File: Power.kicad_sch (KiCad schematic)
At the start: 5 parts, among them U4 LD1117S33TR_SOT223

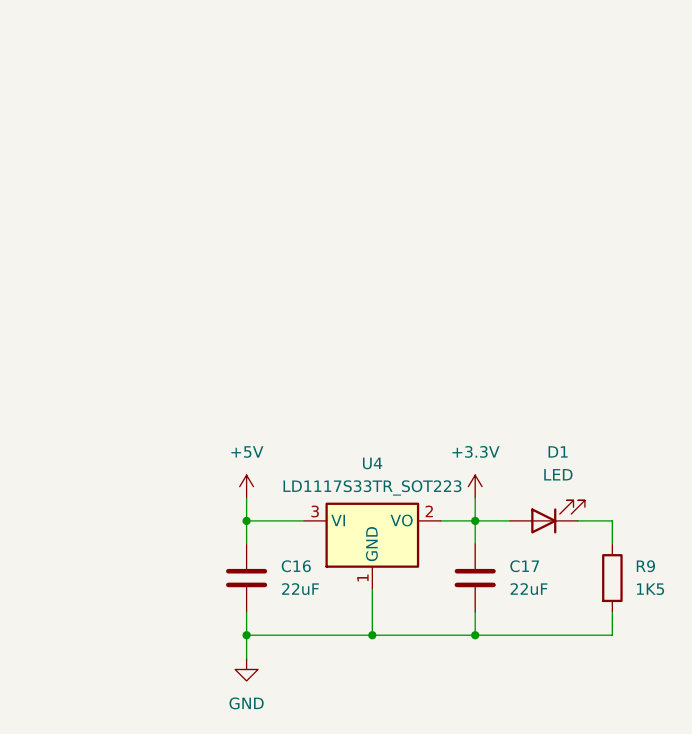
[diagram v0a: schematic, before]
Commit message: MOD : KiCad 8.0.1 -> 9.0.0. ADD : Codec power circuitry.
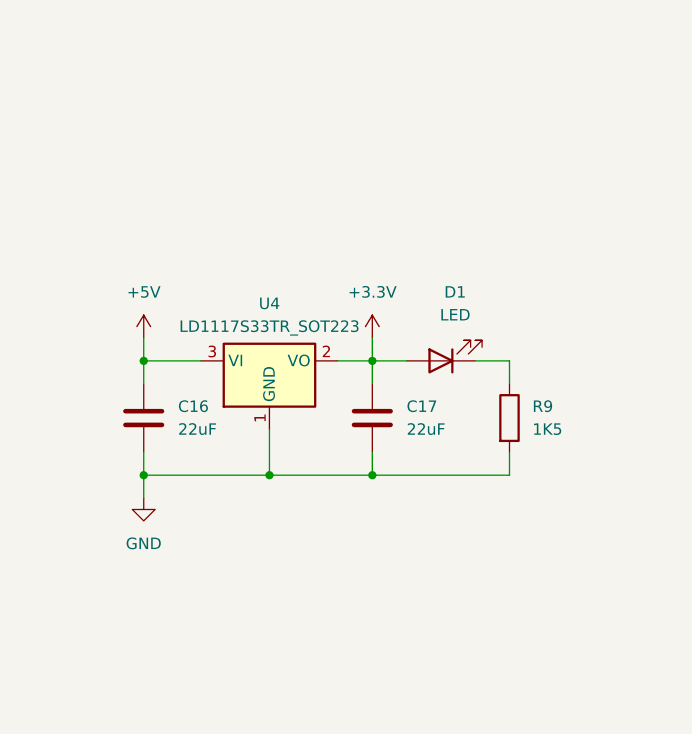
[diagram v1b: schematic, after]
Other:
- moved on the sheet: C16, C17, D1, R9, U4

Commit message: ADD : Footprint assignment. FIX : Various ERC rules.
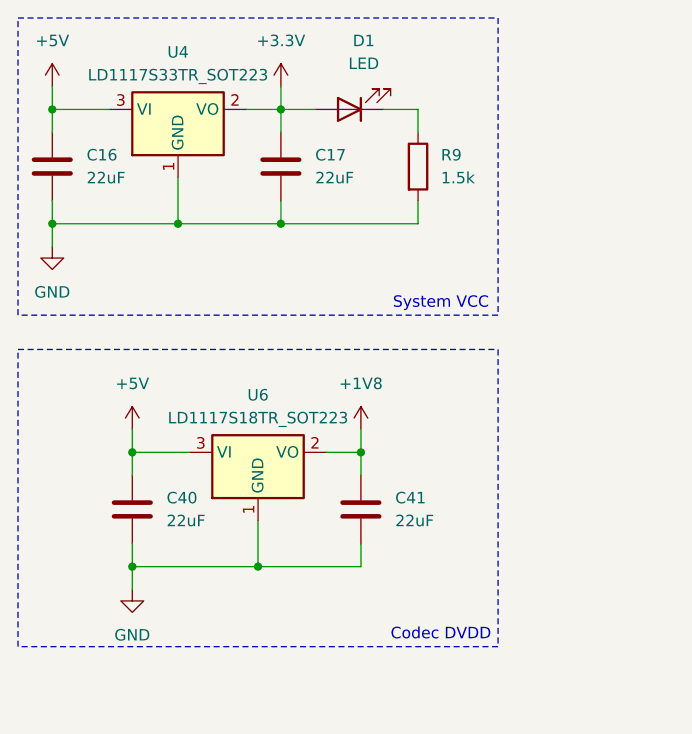
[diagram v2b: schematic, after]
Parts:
- added C40, C41: 22uF, Capacitor_SMD:C_0402_1005Metric, symbol Device:C
- added U6: LD1117S18TR_SOT223, Package_TO_SOT_SMD:SOT-223-3_TabPin2, symbol Regulator_Linear:LD1117S18TR_SOT223
- C16, C17: footprint (none) -> Capacitor_SMD:C_0402_1005Metric
- D1: footprint (none) -> LED_SMD:LED_0402_1005Metric
- R9: value 1K5 -> 1.5k; footprint (none) -> Resistor_SMD:R_0402_1005Metric
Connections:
- net +5V: now also C40.1, U6.3 (VI)
- net GND: now also C40.2, C41.2, U6.1 (GND)
- new net +1V8: C41.1, U6.2 (VO)
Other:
- note added: "Codec DVDD"
- note added: "System VCC"
- moved on the sheet: C16, C17, D1, R9, U4

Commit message: ADD : Rough PCB part placement. MOD : Swapped codec DVDD LDO.
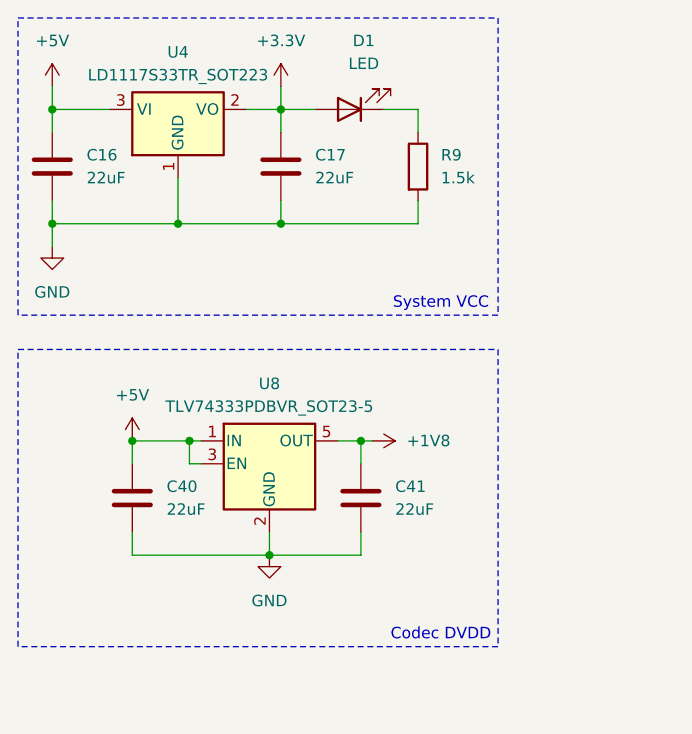
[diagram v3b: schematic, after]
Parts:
- removed U6: LD1117S18TR_SOT223, Package_TO_SOT_SMD:SOT-223-3_TabPin2, symbol Regulator_Linear:LD1117S18TR_SOT223
- added U8: TLV74333PDBVR_SOT23-5, Package_TO_SOT_SMD:SOT-23-5, symbol Regulator_Linear:TLV70218_SOT23-5
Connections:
- net +1V8: now also U8.5 (OUT)
- net +5V: now also U8.1 (IN), U8.3 (EN)
- net GND: now also U8.2 (GND)
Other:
- moved on the sheet: C40, C41
